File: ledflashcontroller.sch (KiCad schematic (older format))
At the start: 23 parts, among them J1 Conn_02x08_Odd_Even, J2 CONN_01X02, J3 CONN_01X02, K1 LDD-1000H, K2 LDD-1000H, P1 V_IN, P2 I2C_HEADER, P3 GPIO_HEADER, P4 V_DIM1, P5 V_DIM2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

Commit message: RTC update
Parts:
- added C7: 100n, Capacitors_SMD:C_0603, symbol C
- added C8: 1u, Capacitors_SMD:C_0603, symbol C
- added J4: Conn_01x02, Pin_Headers:Pin_Header_Straight_1x02_Pitch2.54mm, symbol Conn_01x02
- added U11: DS3231, Housings_SOIC:SOIC-16W_7.5x10.3mm_Pitch1.27mm, symbol DS3231
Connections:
- net +3V3: now also C7.1, C8.1, U11.2 (VCC)
- net GND: now also C7.2, C8.2, J4.1 (Pin_1), U11.10 (NC), U11.11 (NC), U11.12 (NC), U11.13 (GND), U11.5 (NC), U11.6 (NC), U11.7 (NC), U11.8 (NC), U11.9 (NC)
- net SCL: now also U11.16 (SCL)
- net SDA: now also U11.15 (SDA)
- net RTC_SQW: now reaches U1.36 (39_A20)
- net RTC_SQW: now also U11.3 (~INT~/SQW)
- net RTC_RST: now reaches U1.43 (16_A2_scl0_Touch)
- net RTC_RST: now also U11.4 (~RST)
- net RTC_32kHz: now reaches U1.44 (17_A3_sda0_Touch)
- net RTC_32kHz: now also U11.1 (32KHZ)
- new net RTC_VBAT: J4.2 (Pin_2), U11.14 (VBAT)
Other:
- moved on the sheet: J2, J3, P2, P3, R1, R2, R3

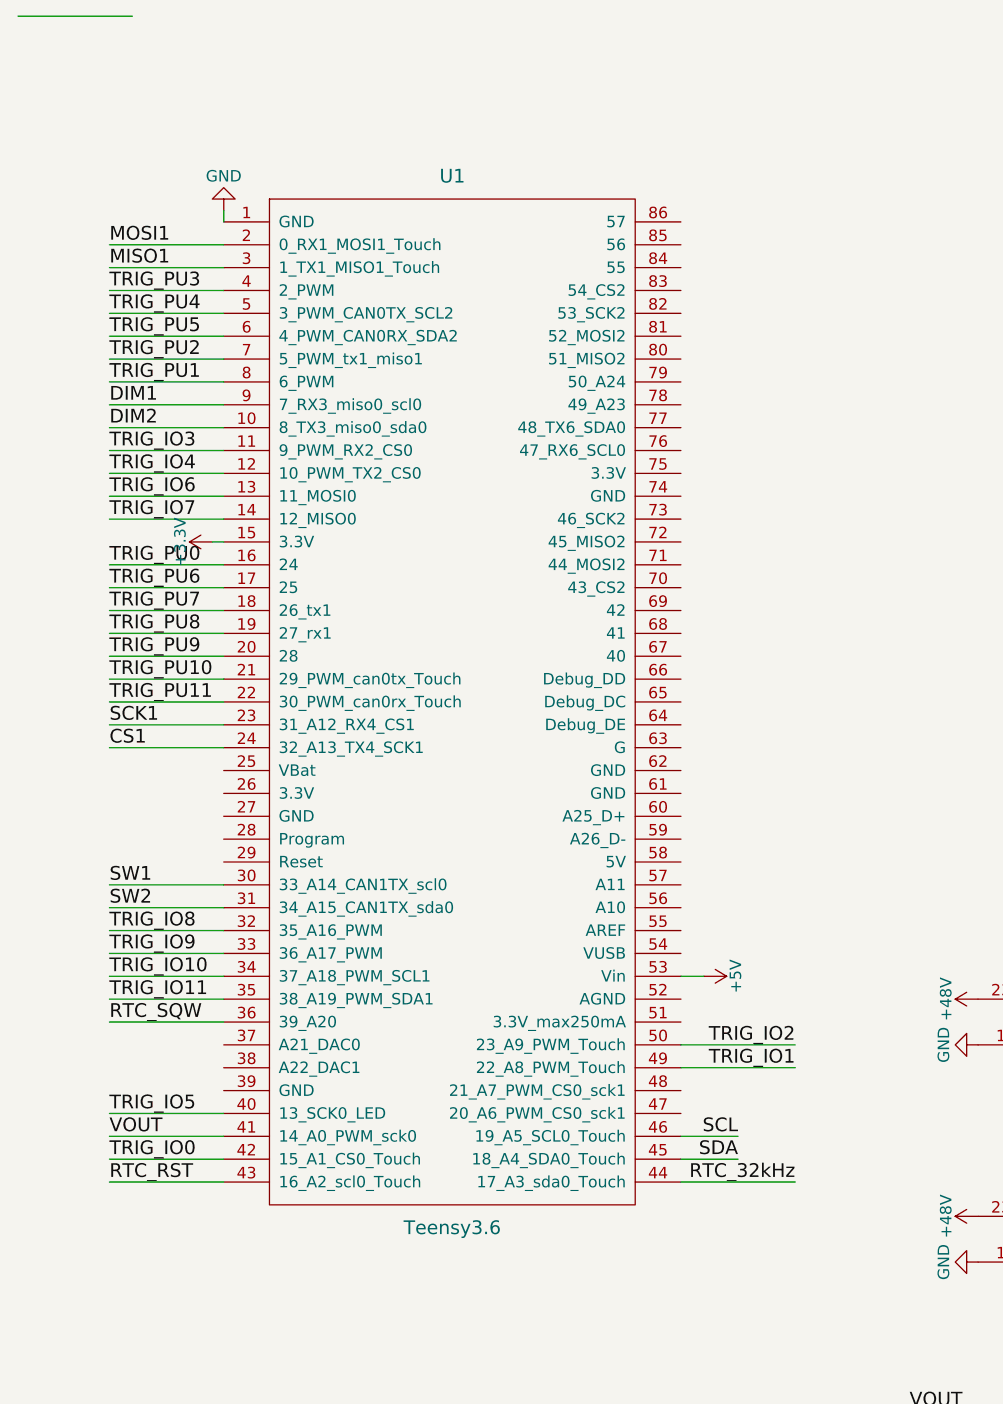
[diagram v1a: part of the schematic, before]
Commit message: Cleanup teensy schematic and remove old custom.lib
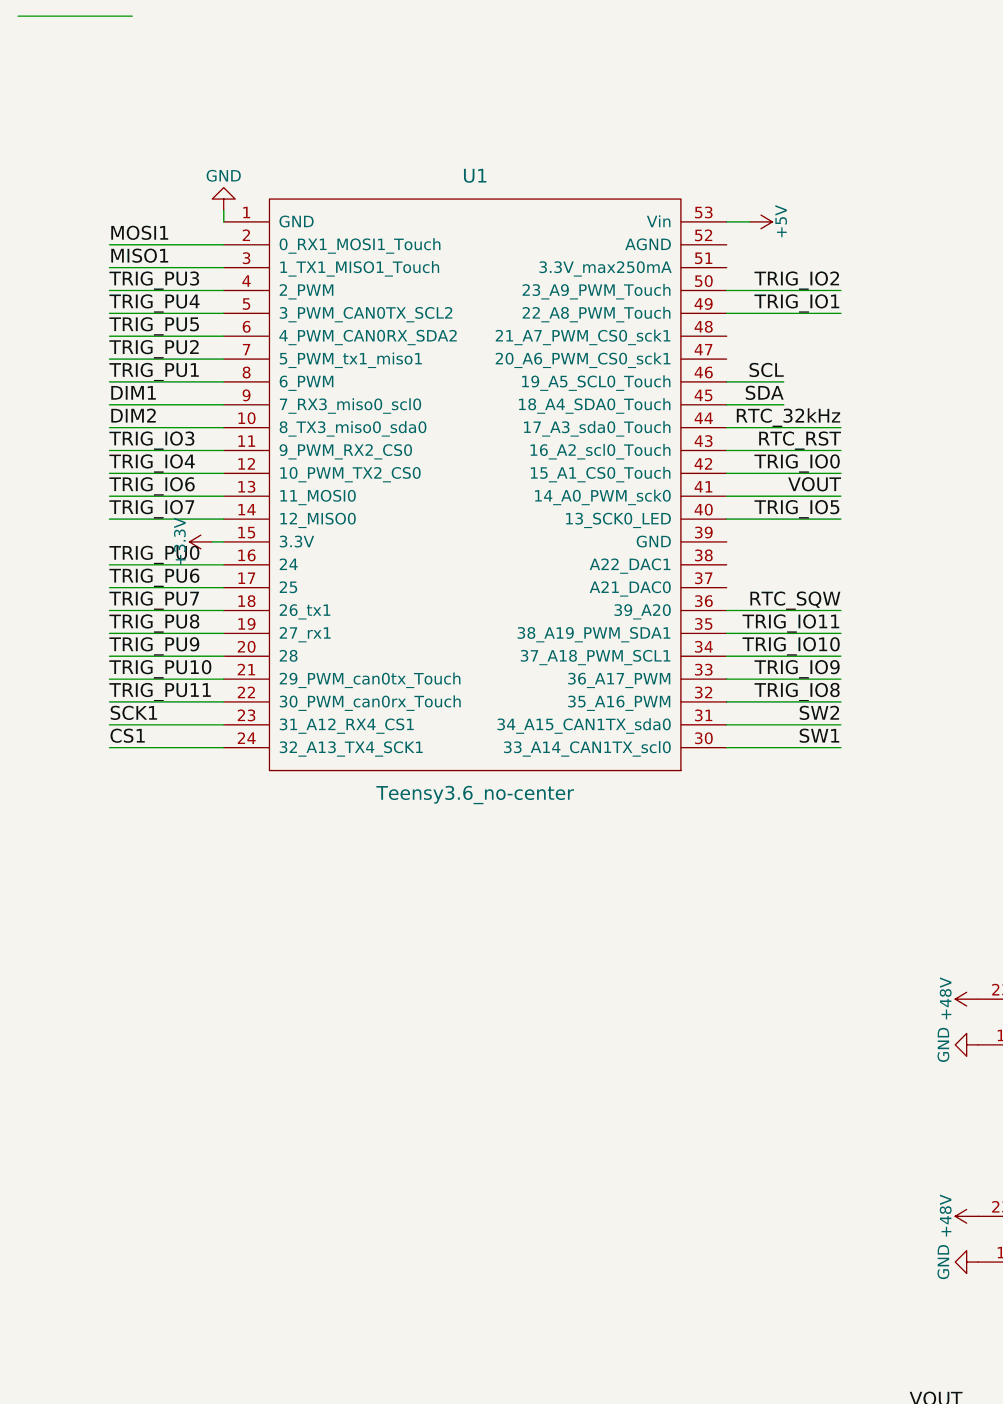
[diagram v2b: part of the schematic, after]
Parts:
- removed U1: Teensy3.6, lib_fp:Teensy35_36_no_center, symbol Teensy3.6
- added U1: Teensy3.6_no-center, lib_fp:Teensy35_36_no-center, symbol Teensy3.6_no-center
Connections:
- net +3V3: now also U1.15 (3.3V)
- net +5V: now also U1.53 (Vin)
- net CS1: now also U1.24 (32_A13_TX4_SCK1)
- net DIM1: now also U1.9 (7_RX3_miso0_scl0)
- net DIM2: now also U1.10 (8_TX3_miso0_sda0)
- net GND: now also U1.1 (GND)
- net MISO1: now also U1.3 (1_TX1_MISO1_Touch)
- net MOSI1: now also U1.2 (0_RX1_MOSI1_Touch)
- net RTC_32kHz: now also U1.44 (17_A3_sda0_Touch)
- net RTC_RST: now also U1.43 (16_A2_scl0_Touch)
- net RTC_SQW: now also U1.36 (39_A20)
- net SCK1: now also U1.23 (31_A12_RX4_CS1)
- net SCL: now also U1.46 (19_A5_SCL0_Touch)
- net SDA: now also U1.45 (18_A4_SDA0_Touch)
- net SW1: now also U1.30 (33_A14_CAN1TX_scl0)
- net SW2: now also U1.31 (34_A15_CAN1TX_sda0)
- net TRIG_IO0: now also U1.42 (15_A1_CS0_Touch)
- net TRIG_IO1: now also U1.49 (22_A8_PWM_Touch)
- net TRIG_IO10: now also U1.34 (37_A18_PWM_SCL1)
- net TRIG_IO11: now also U1.35 (38_A19_PWM_SDA1)
- net TRIG_IO2: now also U1.50 (23_A9_PWM_Touch)
- net TRIG_IO3: now also U1.11 (9_PWM_RX2_CS0)
- net TRIG_IO4: now also U1.12 (10_PWM_TX2_CS0)
- net TRIG_IO5: now also U1.40 (13_SCK0_LED)
- net TRIG_IO6: now also U1.13 (11_MOSI0)
- net TRIG_IO7: now also U1.14 (12_MISO0)
- net TRIG_IO8: now also U1.32 (35_A16_PWM)
- net TRIG_IO9: now also U1.33 (36_A17_PWM)
- net TRIG_PU0: now also U1.16 (24)
- net TRIG_PU1: now also U1.8 (6_PWM)
- net TRIG_PU10: now also U1.21 (29_PWM_can0tx_Touch)
- net TRIG_PU11: now also U1.22 (30_PWM_can0rx_Touch)
- net TRIG_PU2: now also U1.7 (5_PWM_tx1_miso1)
- net TRIG_PU3: now also U1.4 (2_PWM)
- net TRIG_PU4: now also U1.5 (3_PWM_CAN0TX_SCL2)
- net TRIG_PU5: now also U1.6 (4_PWM_CAN0RX_SDA2)
- net TRIG_PU6: now also U1.17 (25)
- net TRIG_PU7: now also U1.18 (26_tx1)
- net TRIG_PU8: now also U1.19 (27_rx1)
- net TRIG_PU9: now also U1.20 (28)
- net VOUT: now also U1.41 (14_A0_PWM_sck0)
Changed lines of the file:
@@
 EESchema Schematic File Version 2
+LIBS:teensy36_no-center
+LIBS:ldd-1000h
 LIBS:maxim
 LIBS:dmc2700
 LIBS:iso1540
 LIBS:74lvc
-LIBS:custom
 LIBS:ledflashcontroller-rescue
 LIBS:power
@@
 L +5V #PWR02
 U 1 1 59810350
-P 3350 4250
-F 0 "#PWR02" H 3350 4100 50  0001 C CNN
-F 1 "+5V" H 3350 4390 50  0000 C CNN
-F 2 "" H 3350 4250 50  0000 C CNN
-F 3 "" H 3350 4250 50  0000 C CNN
-	1    3350 4250
+P 3550 950
+F 0 "#PWR02" H 3550 800 50  0001 C CNN
+F 1 "+5V" H 3550 1090 50  0000 C CNN
+F 2 "" H 3550 950 50  0000 C CNN
+F 3 "" H 3550 950 50  0000 C CNN
+	1    3550 950
 	0    1    1    0
 $EndComp
@@
 Text Label 750  1850 0    60   ~ 0
 DIM2
-Text Label 3500 5050 2    60   ~ 0
+Text Label 3700 1750 2    60   ~ 0
 SDA
-Text Label 3500 4950 2    60   ~ 0
+Text Label 3700 1650 2    60   ~ 0
 SCL
 $Comp
@@
 	1    0    0    -1
 $EndComp
-Text Label 750  3850 0    60   ~ 0
-SW1
-Text Label 750  3950 0    60   ~ 0
-SW2
 $Comp
 L CONN_01X02 P6
@@
 	350  50   850  50
 Wire Wire Line
-	3250 4950 3500 4950
-Wire Wire Line
-	3500 5050 3250 5050
+	3450 1650 3700 1650
+Wire Wire Line
+	3700 1750 3450 1750
 Wire Wire Line
 	9650 2350 9900 2350
@@
 	9450 1950 9650 1950
 Wire Wire Line
-	750  3850 1250 3850
-Wire Wire Line
-	750  3950 1250 3950
-Wire Wire Line
 	750  3250 1250 3250
 Wire Wire Line
@@
 	1250 1050 750  1050
 Wire Wire Line
-	3350 4250 3250 4250
+	3550 950  3450 950
 Wire Wire Line
 	5950 4350 5950 4400
@@
 Wire Wire Line
 	9050 3400 9000 3400
-$Comp
-L Teensy3.6 U1
-U 1 1 59B3BB55
-P 2250 3050
-F 0 "U1" H 2250 5350 60  0000 C CNN
-F 1 "Teensy3.6" H 2250 750 60  0000 C CNN
-F 2 "lib_fp:Teensy35_36_no_center" H 2250 3050 60  0001 C CNN
-F 3 "" H 2250 3050 60  0000 C CNN
-	1    2250 3050
-	1    0    0    -1
-$EndComp
 $Sheet
 S 5450 900  1100 450
@@
 $EndSheet
 Wire Wire Line
-	1250 4950 750  4950
-Text Label 750  4950 0    60   ~ 0
-VOUT
-Wire Wire Line
 	1250 2250 750  2250
 Wire Wire Line
-	1250 4850 750  4850
-Wire Wire Line
 	1250 1950 750  1950
 Wire Wire Line
@@
 Wire Wire Line
 	1250 2150 750  2150
-Wire Wire Line
-	1250 5050 750  5050
 Text Label 750  1950 0    60   ~ 0
 TRIG_IO3
@@
 Text Label 750  2250 0    60   ~ 0
 TRIG_IO7
-Text Label 750  5050 0    60   ~ 0
-TRIG_IO0
-Text Label 750  4850 0    60   ~ 0
-TRIG_IO5
-Wire Wire Line
-	3250 4550 3750 4550
-Wire Wire Line
-	3250 4650 3750 4650
-Text Label 3750 4650 2    60   ~ 0
+Wire Wire Line
+	3450 1250 3950 1250
+Wire Wire Line
+	3450 1350 3950 1350
+Text Label 3950 1350 2    60   ~ 0
 TRIG_IO1
-Text Label 3750 4550 2    60   ~ 0
+Text Label 3950 1250 2    60   ~ 0
 TRIG_IO2
-Wire Wire Line
-	1250 4350 750  4350
-Wire Wire Line
-	1250 4050 750  4050
-Wire Wire Line
-	1250 4150 750  4150
-Wire Wire Line
-	1250 4250 750  4250
-Text Label 750  4050 0    60   ~ 0
-TRIG_IO8
-Text Label 750  4150 0    60   ~ 0
-TRIG_IO9
-Text Label 750  4250 0    60   ~ 0
-TRIG_IO10
-Text Label 750  4350 0    60   ~ 0
-TRIG_IO11
 Wire Wire Line
 	1250 1550 750  1550
@@
 $EndComp
 Wire Wire Line
-	1250 4450 750  4450
-Text Label 750  4450 0    60   ~ 0
-RTC_SQW
-Wire Wire Line
-	1250 5150 750  5150
-Wire Wire Line
-	3250 5150 3750 5150
-Text Label 750  5150 0    60   ~ 0
-RTC_RST
-Text Label 3750 5150 2    60   ~ 0
+	3450 1850 3950 1850
+Text Label 3950 1850 2    60   ~ 0
 RTC_32kHz
 Wire Wire Line
@@
 Wire Wire Line
 	10500 6200 10050 6200
+$Comp
+L Teensy3.6_no-center U1
+U 1 1 59F0CB59
+P 2350 3050
+F 0 "U1" H 2350 5350 60  0000 C CNN
+F 1 "Teensy3.6_no-center" H 2350 2650 60  0000 C CNN
+F 2 "lib_fp:Teensy35_36_no-center" H 2250 3050 60  0001 C CNN
+F 3 "" H 2250 3050 60  0000 C CNN
+	1    2350 3050
+	1    0    0    -1
+$EndComp
+Text Label 3950 3250 2    60   ~ 0
+SW1
+Text Label 3950 3150 2    60   ~ 0
+SW2
+Wire Wire Line
+	3950 3250 3450 3250
+Wire Wire Line
+	3950 3150 3450 3150
+Wire Wire Line
+	3450 2150 3950 2150
+Text Label 3950 2150 2    60   ~ 0
+VOUT
+Wire Wire Line
+	3450 2250 3950 2250
+Wire Wire Line
+	3450 2050 3950 2050
+Text Label 3950 2050 2    60   ~ 0
+TRIG_IO0
+Text Label 3950 2250 2    60   ~ 0
+TRIG_IO5
+Wire Wire Line
+	3450 2750 3950 2750
+Wire Wire Line
+	3450 3050 3950 3050
+Wire Wire Line
+	3450 2950 3950 2950
+Wire Wire Line
+	3450 2850 3950 2850
+Text Label 3950 3050 2    60   ~ 0
+TRIG_IO8
+Text Label 3950 2950 2    60   ~ 0
+TRIG_IO9
+Text Label 3950 2850 2    60   ~ 0
+TRIG_IO10
+Text Label 3950 2750 2    60   ~ 0
+TRIG_IO11
+Wire Wire Line
+	3450 2650 3950 2650
+Text Label 3950 2650 2    60   ~ 0
+RTC_SQW
+Wire Wire Line
+	3450 1950 3950 1950
+Text Label 3950 1950 2    60   ~ 0
+RTC_RST
 $EndSCHEMATC

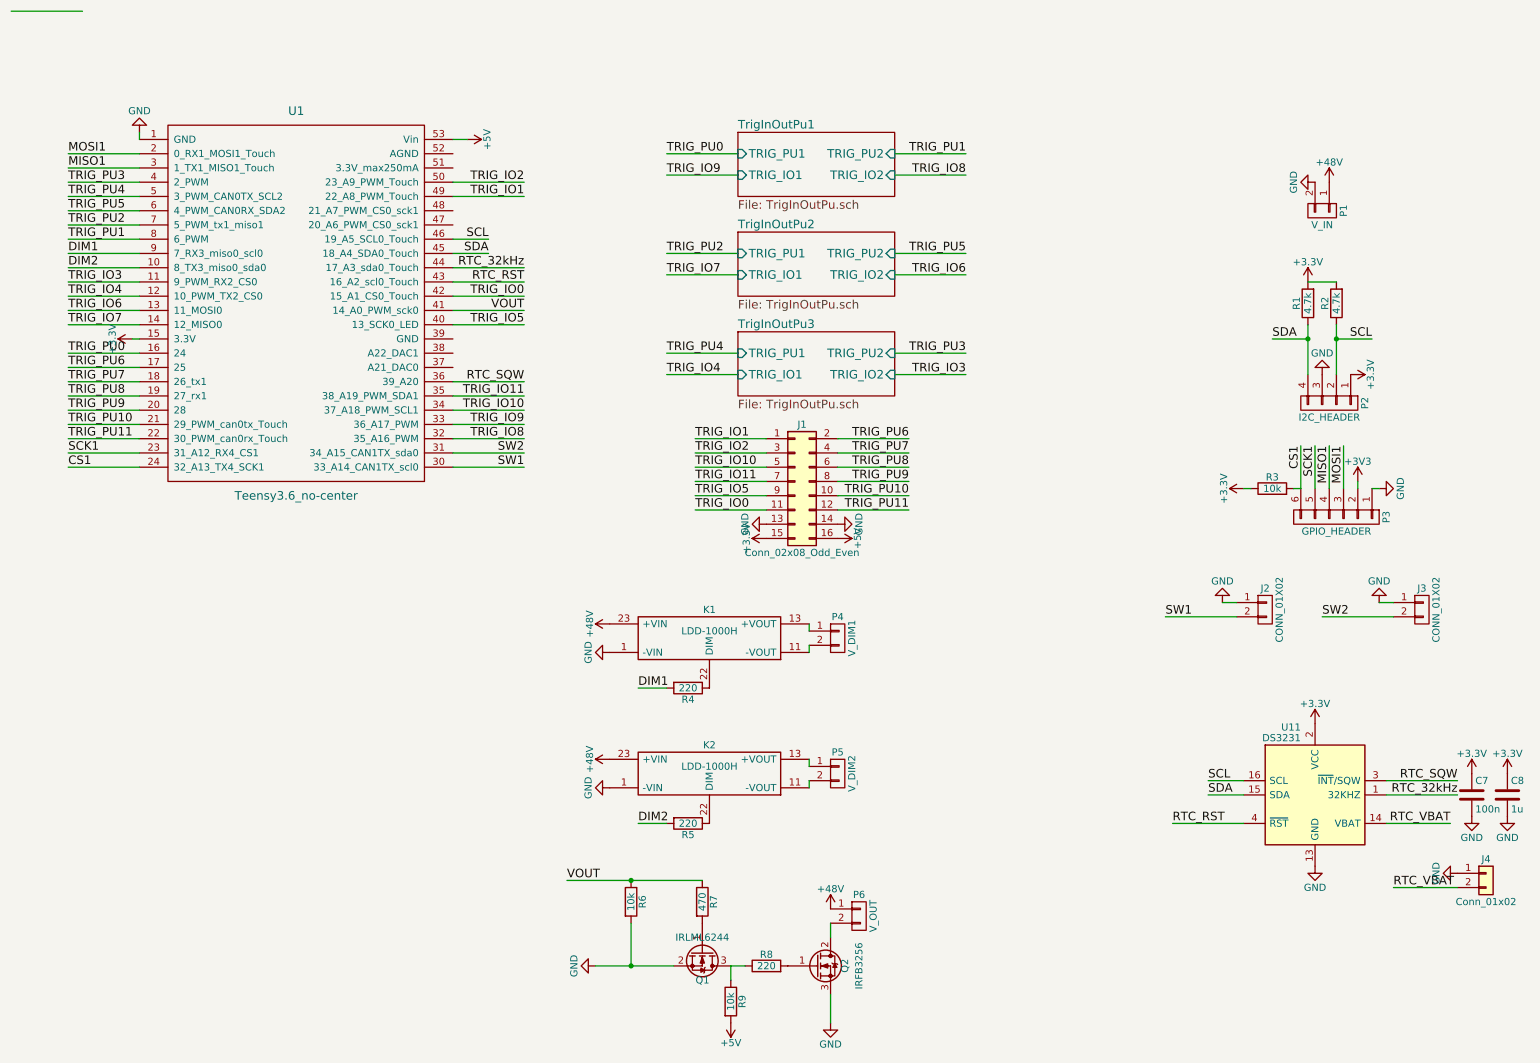
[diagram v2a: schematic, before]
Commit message: Add 2nd teensy ground and rotate mosfet. Fixes #3
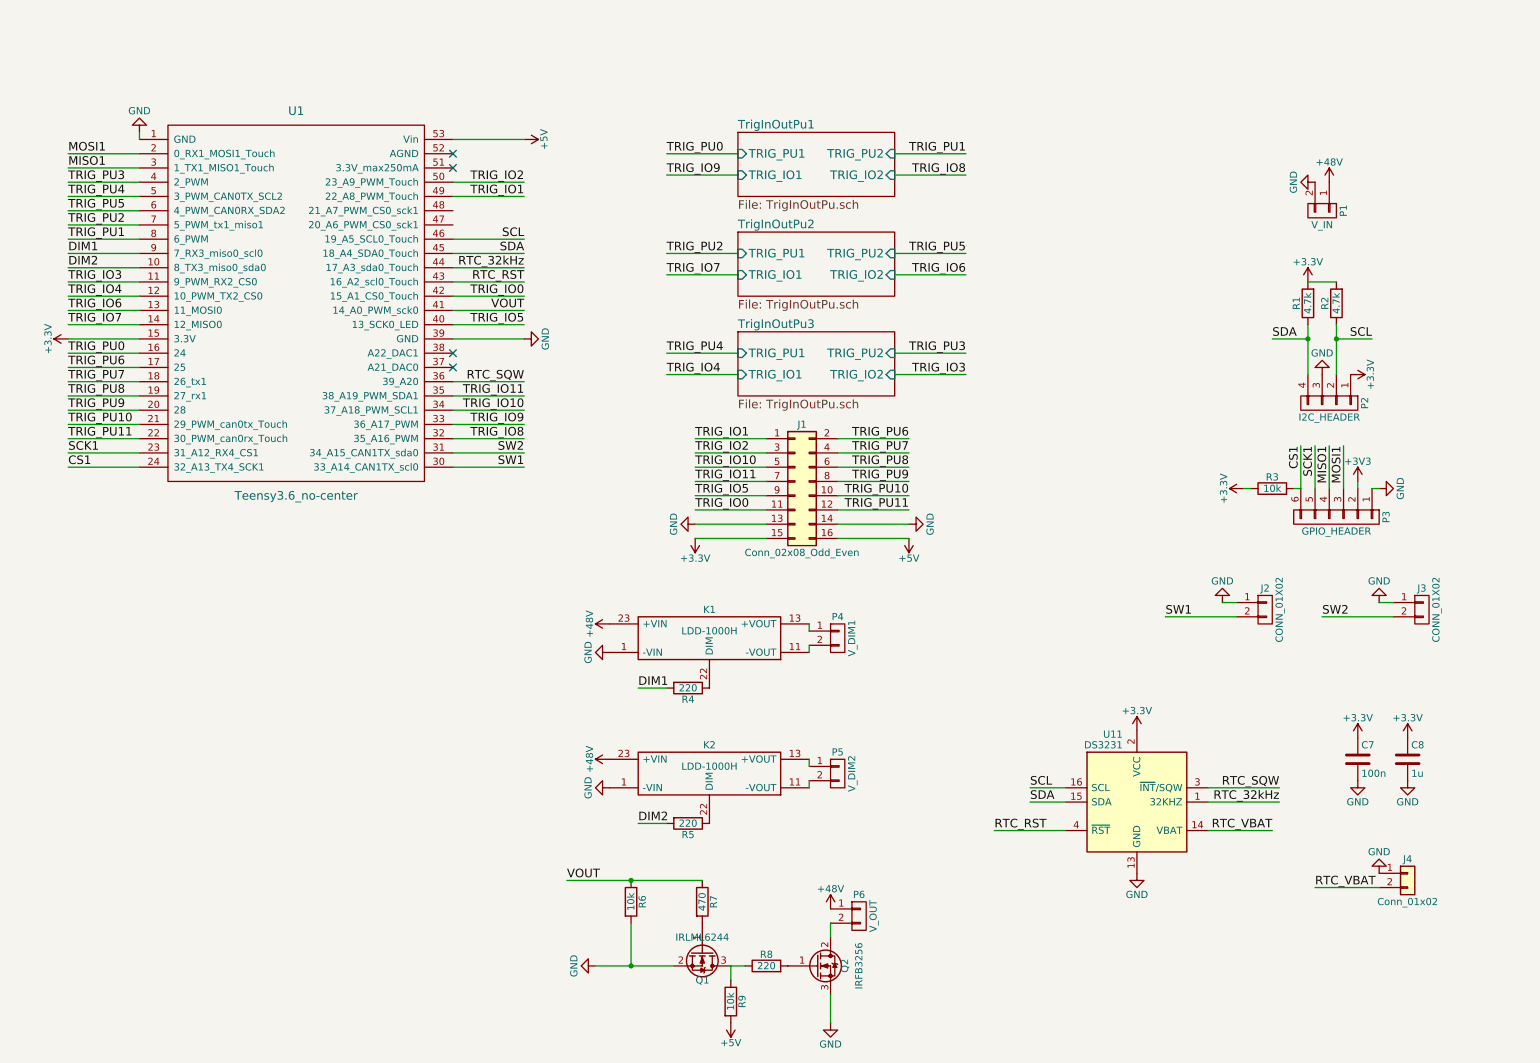
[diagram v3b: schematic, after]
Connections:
- net GND: now also U1.39 (GND)
- no-connect marks 0 -> 4
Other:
- moved on the sheet: C7, C8, J4, U11

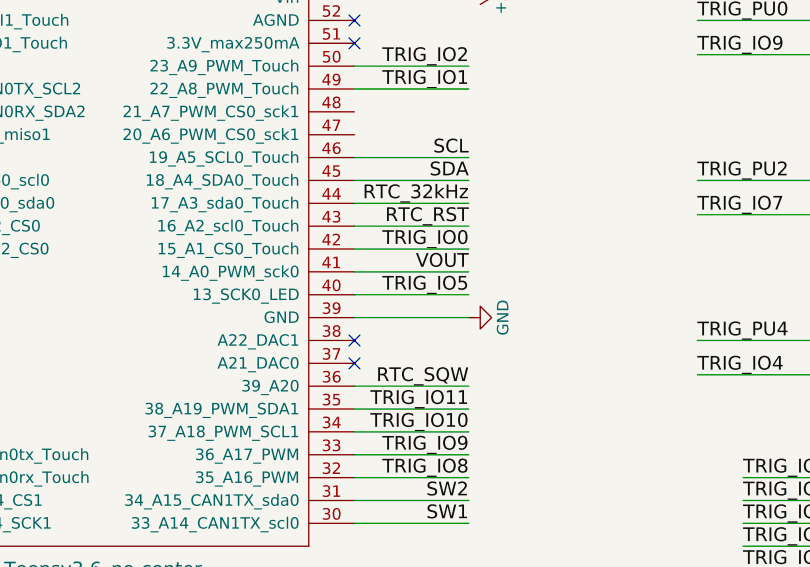
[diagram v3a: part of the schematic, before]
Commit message: Switched RTC_SQW and RTC_32kHz for improved routing
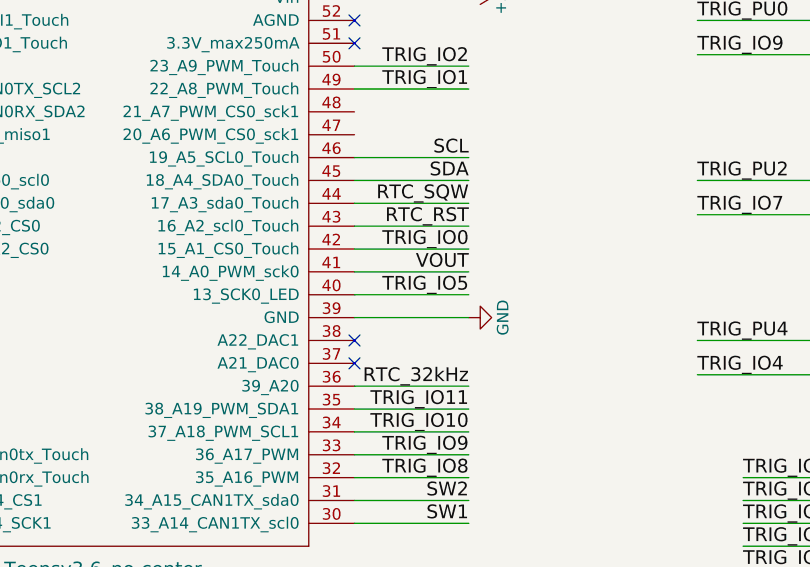
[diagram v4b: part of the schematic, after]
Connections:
- net RTC_32kHz: now also U1.36 (39_A20); no longer U1.44 (17_A3_sda0_Touch)
- net RTC_SQW: now also U1.44 (17_A3_sda0_Touch); no longer U1.36 (39_A20)
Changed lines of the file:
@@
 	3450 1850 3950 1850
 Text Label 3950 1850 2    60   ~ 0
-RTC_32kHz
+RTC_SQW
 Wire Wire Line
 	8750 5600 9250 5600
@@
 	3450 2650 3950 2650
 Text Label 3950 2650 2    60   ~ 0
-RTC_SQW
+RTC_32kHz
 Wire Wire Line
 	3450 1950 3950 1950
